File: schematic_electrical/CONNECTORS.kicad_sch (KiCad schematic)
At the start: 9 parts, among them J12 Conn_01x03, J13 Conn_01x02, J14 Conn_02x04_Odd_Even, J15 Conn_01x02, J16 Conn_01x03, J18 Conn_02x04_Odd_Even, J3 Conn_01x02

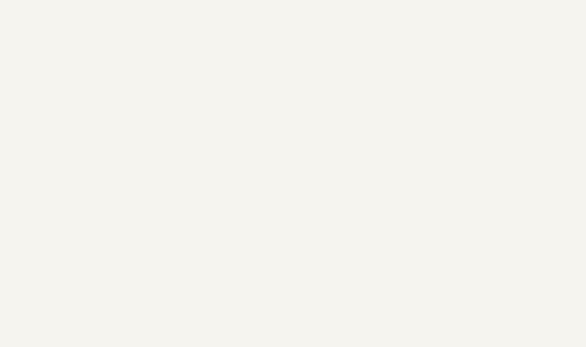
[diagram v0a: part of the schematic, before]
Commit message: Pylon schmatic: clarify filenames and add orange text to avoid confusing other similar schematic pages.
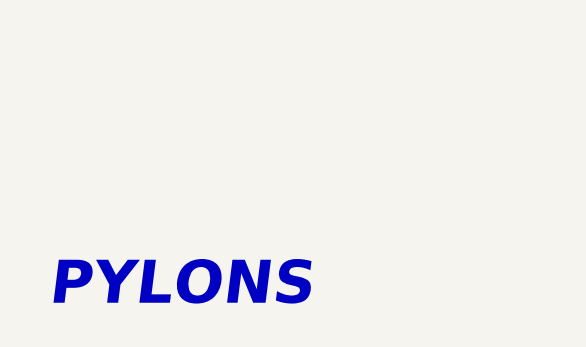
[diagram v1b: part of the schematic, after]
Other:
- note added: "PYLONS"
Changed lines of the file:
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@@
+		)
+	)
+	(text "PYLONS"
+		(exclude_from_sim no)
+		(at 30.226 157.48 0)
+		(effects
+			(font
+				(size 4.7752 4.7752)
+				(thickness 0.955)
+				(bold yes)
+				(italic yes)
+				(color 255 153 0 1)
+			)
 		)
 	)
@@
 		)
 		(instances
-			(project "high_striker_boosh"
+			(project "pylons_boosh_remote_reciver"
 				(path "/f3653ac0-a28a-4ee8-bcf5-236139001455/d08cb7b6-6190-46a9-b97e-3e5f70878a10"
 					(reference "#PWR060")
@@
 		)
 		(instances
-			(project "high_striker_boosh"
+			(project "pylons_boosh_remote_reciver"
 				(path "/f3653ac0-a28a-4ee8-bcf5-236139001455/d08cb7b6-6190-46a9-b97e-3e5f70878a10"
 					(reference "J16")
@@
 		)
 		(instances
-			(project "high_striker_boosh"
+			(project "pylons_boosh_remote_reciver"
 				(path "/f3653ac0-a28a-4ee8-bcf5-236139001455/d08cb7b6-6190-46a9-b97e-3e5f70878a10"
 					(reference "J3")
@@
 		)
 		(instances
-			(project "high_striker_boosh"
+			(project "pylons_boosh_remote_reciver"
 				(path "/f3653ac0-a28a-4ee8-bcf5-236139001455/d08cb7b6-6190-46a9-b97e-3e5f70878a10"
 					(reference "#PWR047")
@@
 		)
 		(instances
-			(project "high_striker_boosh"
+			(project "pylons_boosh_remote_reciver"
 				(path "/f3653ac0-a28a-4ee8-bcf5-236139001455/d08cb7b6-6190-46a9-b97e-3e5f70878a10"
 					(reference "J13")
@@
 		)
 		(instances
-			(project "high_striker_boosh"
+			(project "pylons_boosh_remote_reciver"
 				(path "/f3653ac0-a28a-4ee8-bcf5-236139001455/d08cb7b6-6190-46a9-b97e-3e5f70878a10"
 					(reference "PS1")
@@
 		)
 		(instances
-			(project "high_striker_boosh"
+			(project "pylons_boosh_remote_reciver"
 				(path "/f3653ac0-a28a-4ee8-bcf5-236139001455/d08cb7b6-6190-46a9-b97e-3e5f70878a10"
 					(reference "J12")
@@
 		)
 		(instances
-			(project "high_striker_boosh"
+			(project "pylons_boosh_remote_reciver"
 				(path "/f3653ac0-a28a-4ee8-bcf5-236139001455/d08cb7b6-6190-46a9-b97e-3e5f70878a10"
 					(reference "#PWR053")
@@
 		)
 		(instances
-			(project "high_striker_boosh"
+			(project "pylons_boosh_remote_reciver"
 				(path "/f3653ac0-a28a-4ee8-bcf5-236139001455/d08cb7b6-6190-46a9-b97e-3e5f70878a10"
 					(reference "J18")
@@
 		)
 		(instances
-			(project "high_striker_boosh"
+			(project "pylons_boosh_remote_reciver"
 				(path "/f3653ac0-a28a-4ee8-bcf5-236139001455/d08cb7b6-6190-46a9-b97e-3e5f70878a10"
 					(reference "L1")
@@
 		)
 		(instances
-			(project "high_striker_boosh"
+			(project "pylons_boosh_remote_reciver"
 				(path "/f3653ac0-a28a-4ee8-bcf5-236139001455/d08cb7b6-6190-46a9-b97e-3e5f70878a10"
 					(reference "#PWR054")
@@
 		)
 		(instances
-			(project "high_striker_boosh"
+			(project "pylons_boosh_remote_reciver"
 				(path "/f3653ac0-a28a-4ee8-bcf5-236139001455/d08cb7b6-6190-46a9-b97e-3e5f70878a10"
 					(reference "#PWR055")
@@
 		)
 		(instances
-			(project "high_striker_boosh"
+			(project "pylons_boosh_remote_reciver"
 				(path "/f3653ac0-a28a-4ee8-bcf5-236139001455/d08cb7b6-6190-46a9-b97e-3e5f70878a10"
 					(reference "J14")
@@
 		)
 		(instances
-			(project "high_striker_boosh"
+			(project "pylons_boosh_remote_reciver"
 				(path "/f3653ac0-a28a-4ee8-bcf5-236139001455/d08cb7b6-6190-46a9-b97e-3e5f70878a10"
 					(reference "J15")
@@
 		)
 		(instances
-			(project "high_striker_boosh"
+			(project "pylons_boosh_remote_reciver"
 				(path "/f3653ac0-a28a-4ee8-bcf5-236139001455/d08cb7b6-6190-46a9-b97e-3e5f70878a10"
 					(reference "#PWR059")

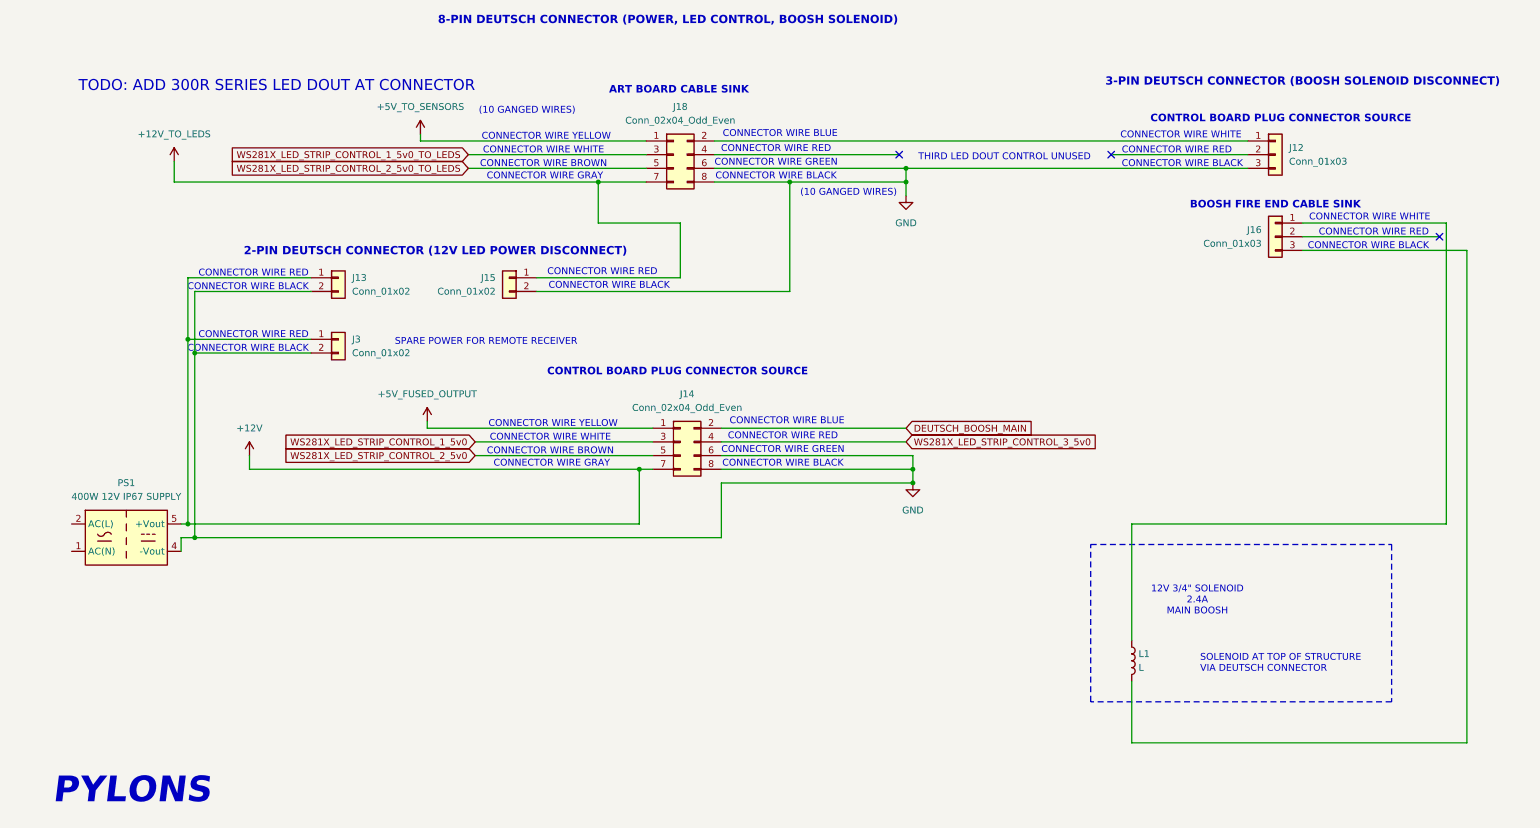
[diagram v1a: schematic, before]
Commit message: Schematic for fabrication. New symbols
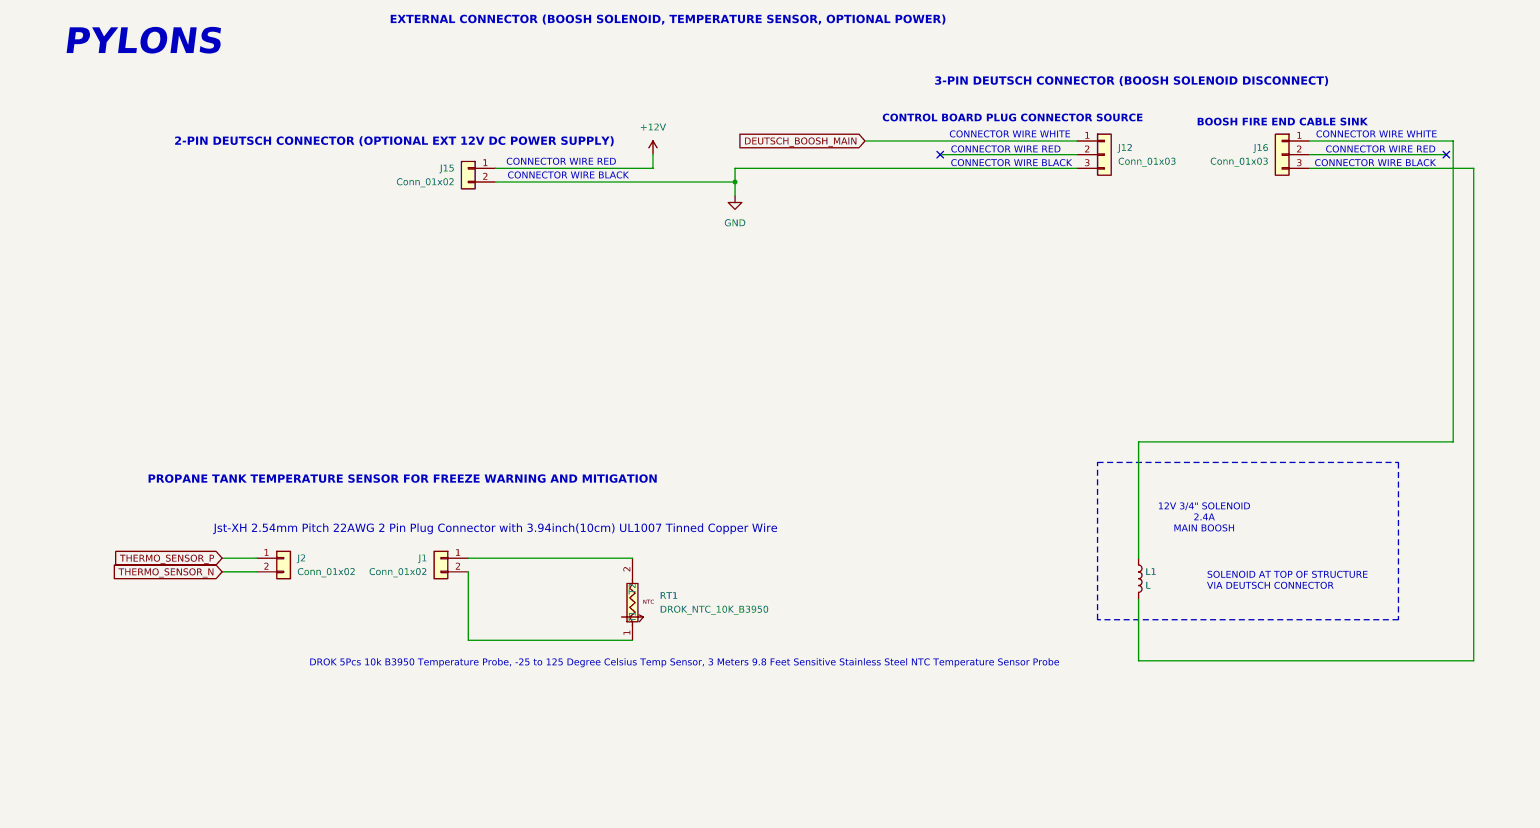
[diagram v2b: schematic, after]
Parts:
- removed J13, J3: Conn_01x02, symbol Connector_Generic:Conn_01x02
- removed J14, J18: Conn_02x04_Odd_Even, symbol Connector_Generic:Conn_02x04_Odd_Even
- removed PS1: 400W 12V IP67 SUPPLY, Converter_ACDC:Converter_ACDC_Recom_RAC20-xxSK_THT, symbol Converter_ACDC:RAC20-12SK
- added J1, J2: Conn_01x02, symbol Connector_Generic:Conn_01x02
- added RT1: DROK_NTC_10K_B3950, symbol drok_ntc_10k_b3950:DROK_NTC_10K_B3950
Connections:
- net +12V_TO_LEDS is gone; now on net +12V: J15.1 (Pin_1)
- net DEUTSCH_BOOSH_MAIN: now also J12.1 (Pin_1)
- new net: J1.2 (Pin_2), RT1.1 (T1)
- new net: J1.1 (Pin_1), RT1.2 (T2)
- new net THERMO_SENSOR_N: J2.2 (Pin_2)
- new net THERMO_SENSOR_P: J2.1 (Pin_1)
- no-connect marks 3 -> 2
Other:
- note added: "2-PIN DEUTSCH CONNECTOR (OPTIONAL EXT 12V DC POWER SUPPLY)"
- note added: "DROK 5Pcs 10k B3950 Temperature Probe, -25 to 125 Degree Celsius Temp Sensor, 3 Meters 9.8 Feet Sensitive Stainless Steel NTC Temperature Sensor Probe"
- note added: "EXTERNAL CONNECTOR (BOOSH SOLENOID, TEMPERATURE SENSOR, OPTIONAL POWER)"
- note added: "Jst-XH 2.54mm Pitch 22AWG 2 Pin Plug Connector with 3.94inch(10cm) UL1007 Tinned Copper Wire"
- note added: "PROPANE TANK TEMPERATURE SENSOR FOR FREEZE WARNING AND MITIGATION"
- note removed: "(10 GANGED WIRES)"
- note removed: "2-PIN DEUTSCH CONNECTOR (12V LED POWER DISCONNECT)"
- note removed: "8-PIN DEUTSCH CONNECTOR (POWER, LED CONTROL, BOOSH SOLENOID)"
- note removed: "ART BOARD CABLE SINK"
- note removed: "CONNECTOR WIRE BLUE"
- note removed: "CONNECTOR WIRE BROWN"
- note removed: "CONNECTOR WIRE GRAY"
- note removed: "CONNECTOR WIRE GREEN"
- note removed: "CONNECTOR WIRE YELLOW"
- note removed: "SPARE POWER FOR REMOTE RECEIVER"
- note removed: "THIRD LED DOUT CONTROL UNUSED"
- note removed: "TODO: ADD 300R SERIES LED DOUT AT CONNECTOR"
- moved on the sheet: J12, J15, J16, L1

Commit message: Schematic symbols and cleanup for building board
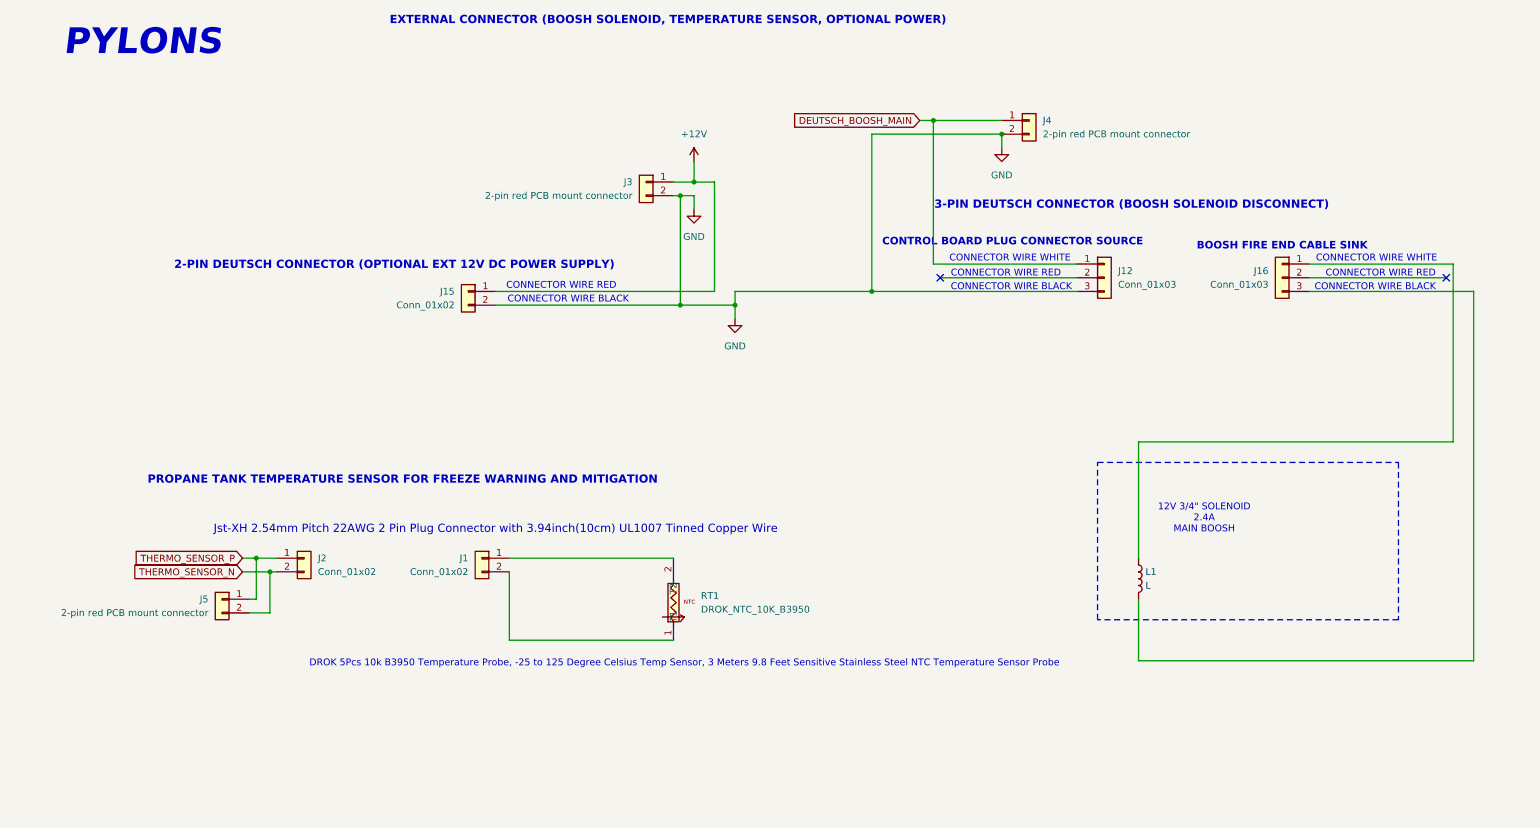
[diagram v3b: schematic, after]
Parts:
- added J3, J4, J5: 2-pin red PCB mount connector, symbol Connector_Generic:Conn_01x02
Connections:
- net +12V: now also J3.1 (Pin_1)
- net DEUTSCH_BOOSH_MAIN: now also J4.1 (Pin_1)
- net GND: now also J3.2 (Pin_2), J4.2 (Pin_2)
- net THERMO_SENSOR_N: now also J5.2 (Pin_2)
- net THERMO_SENSOR_P: now also J5.1 (Pin_1)
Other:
- note removed: "SOLENOID AT TOP OF STRUCTURE VIA DEUTSCH CONNECTOR"
- moved on the sheet: J1, J12, J15, J16, J2, RT1
